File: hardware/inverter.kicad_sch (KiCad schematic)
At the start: 18 parts, among them U2 DRV8262DDWR, U3 TLC555IDR

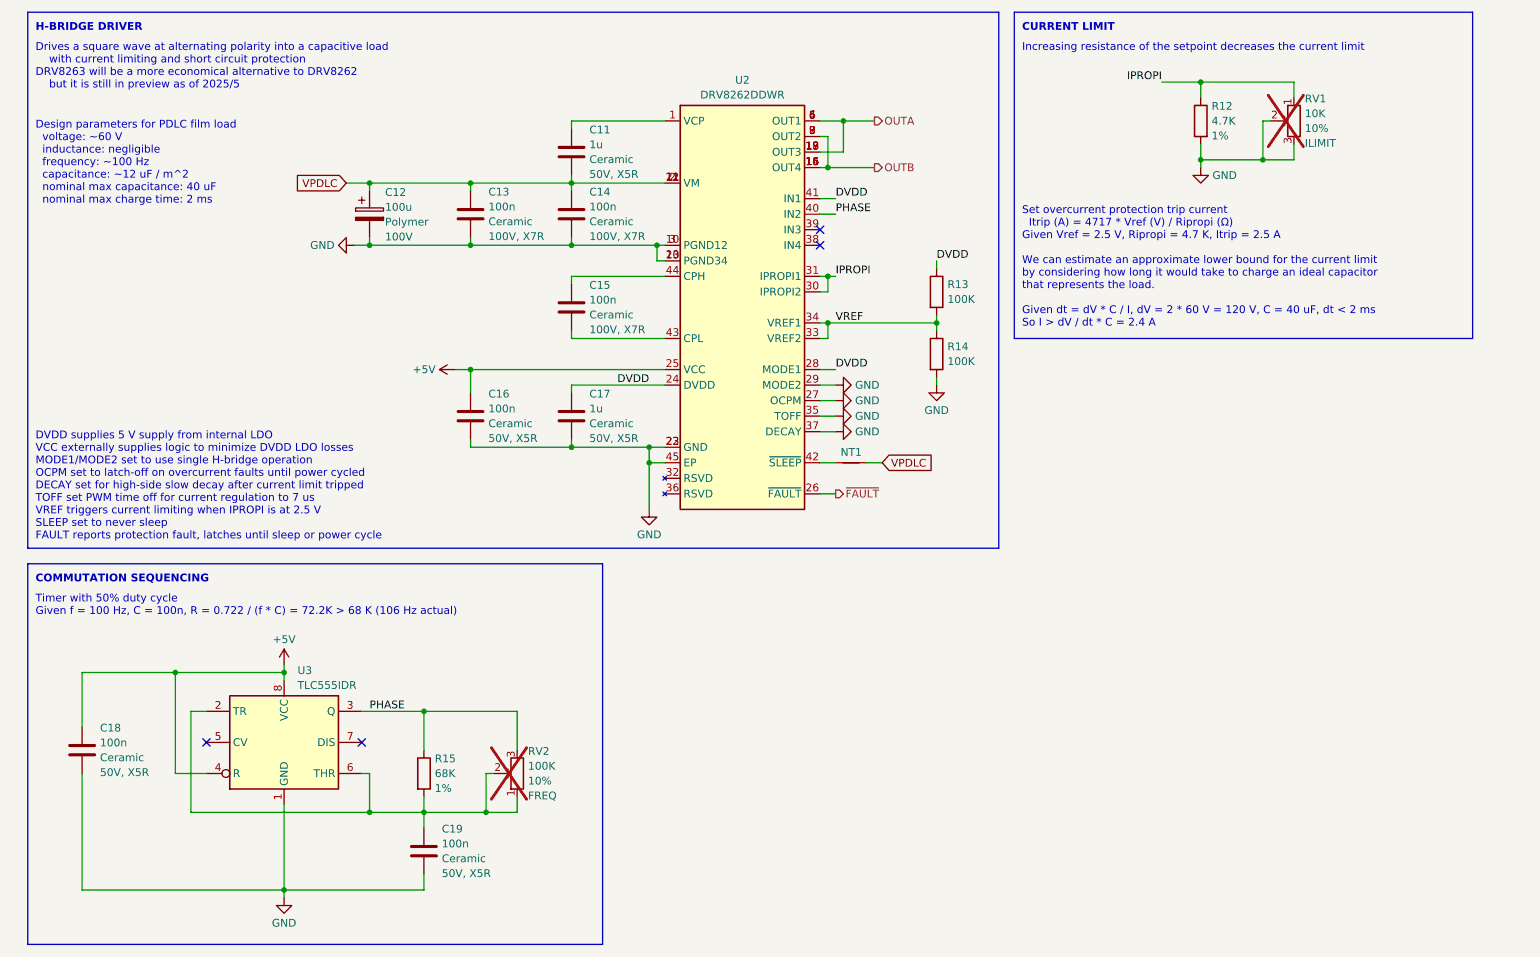
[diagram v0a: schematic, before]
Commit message: Revised layout using LM5108 and discrete FETs
LM5108 is less expensive but it requires more board area.  In lieu of
active current limiting, we rely on the LM5158 hiccup overload
protection.  The FETs are intentionally oversized to handle large
current pulses when switching the polarity of the capacitive load.

This design is complete and ready for manufacture.
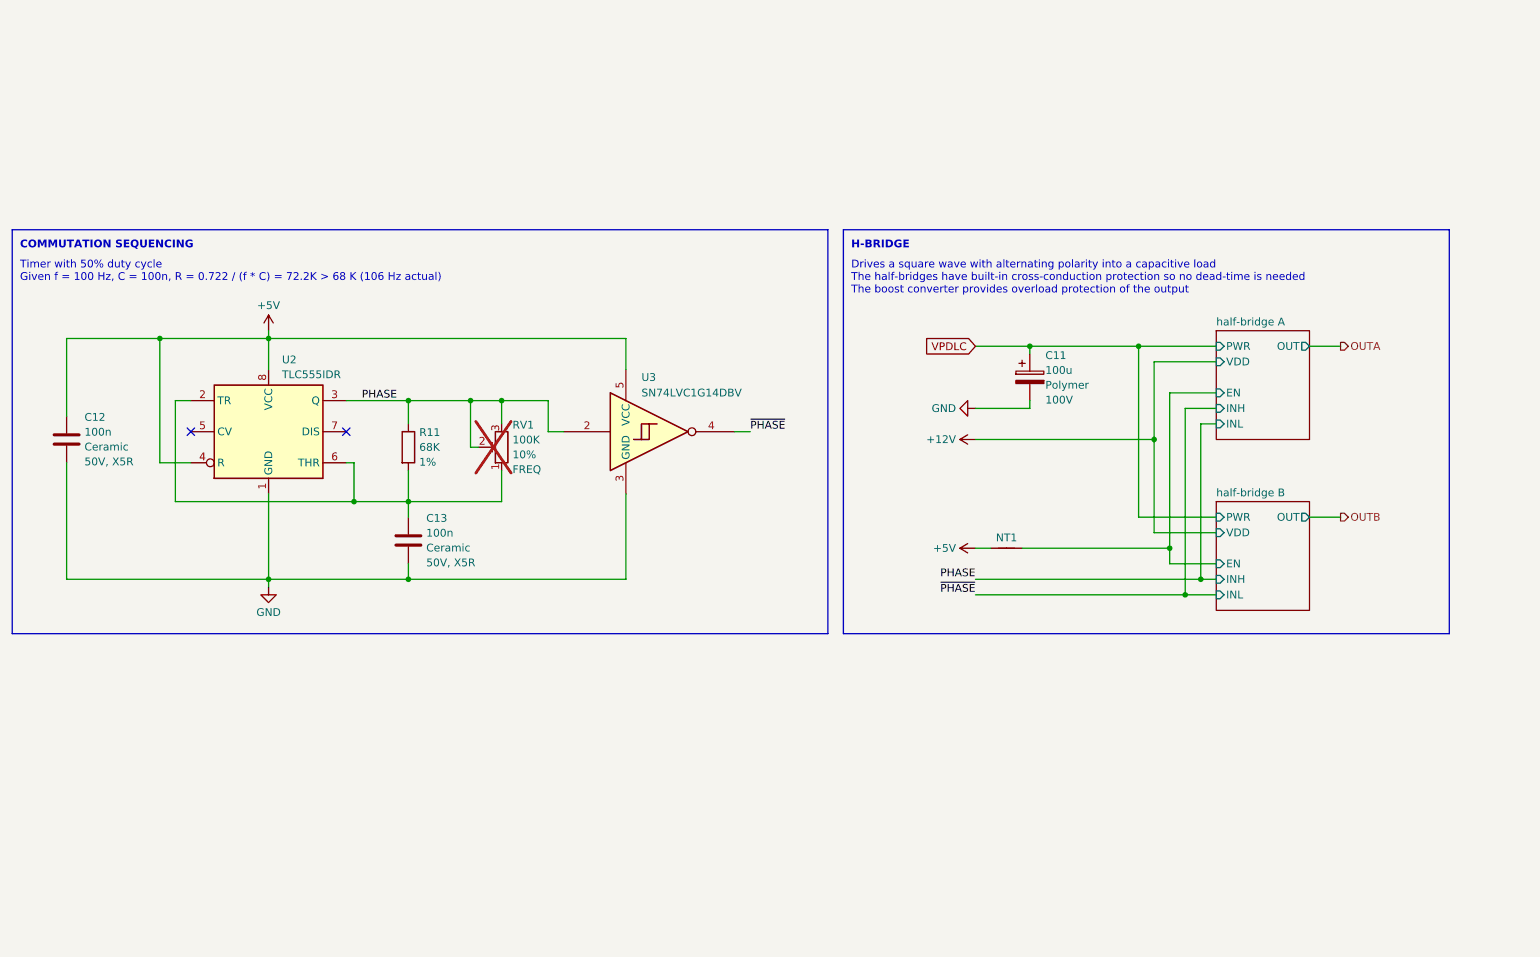
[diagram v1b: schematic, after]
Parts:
- removed C11, C17: 1u, Capacitor_SMD:C_0603_1608Metric, symbol Device:C
- removed C12: 100u, Capacitor_THT:CP_Radial_D10.0mm_P5.00mm, symbol Device:C_Polarized
- removed C13, C14, C15: 100n, Capacitor_SMD:C_0805_2012Metric, symbol Device:C
- removed C16: 100n, Capacitor_SMD:C_0603_1608Metric, symbol Device:C
- removed R12: 4.7K, Resistor_SMD:R_0603_1608Metric, symbol Device:R
- removed R13, R14: 100K, Resistor_SMD:R_0603_1608Metric, symbol Device:R
- removed RV1: 10K, 3362P-1-502LF:TRIM_3362P-1-502LF, symbol Device:R_Potentiometer_Trim
- removed U2: DRV8262DDWR, Package_SO:HTSSOP-44-1EP_6.1x14mm_P0.635mm_EP5.2x14mm_Mask4.31x8.26mm, symbol DRV8262:DRV8262DDWR
- added C11: 100u, Capacitor_THT:CP_Radial_D10.0mm_P5.00mm, symbol Device:C_Polarized
- added U3: SN74LVC1G14DBV, Package_TO_SOT_SMD:SOT-23-5, symbol 74xGxx:SN74LVC1G14DBV
- renumbered C18 to C12, C19 to C13, R15 to R11, RV2 to RV1, U3 to U2
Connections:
- net +5V: now also NT1.1, U3.5 (VCC)
- net GND: now also C11.2, U3.3 (GND)
- net PHASE: now also RV1.2, U3.2
- net VPDLC: now also C11.1; no longer NT1.2
- net at C13.1, R11.2, RV1.1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: no longer RV1.2
- new net half-bridge A/EN: NT1.2
- new net ~{PHASE}: U3.4
- no-connect marks 4 -> 2
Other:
- added sheet half-bridge A (half-bridge.kicad_sch)
- added sheet half-bridge B (half-bridge.kicad_sch)
- note added: "Drives a square wave with alternating polarity into a capacitive load The half-bridges have built-in cross-conduction protection so no dead-time is needed The boost converter provides overload protection of the output"
- note added: "H-BRIDGE"
- note removed: "CURRENT LIMIT"
- note removed: "DVDD supplies 5 V supply from internal LDO VCC externally supplies logic to minimize DVDD LDO losses MODE1/MODE2 set to use single H-bridge operation OCPM set to latch-off on overcurrent faults until power cycled DECAY set for high-side slow decay after current limit tripped TOFF set PWM time off for current regulation to 7 us VREF triggers current limiting when IPROPI is at 2.5 V SLEEP set to ne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"
- note removed: "Design parameters for PDLC film load voltage: ~60 V inductance: negligible frequency: ~100 Hz capacitance: ~12 uF / m^2 nominal max capacitance: 40 uF nominal max charge time: 2 ms"
- note removed: "Drives a square wave at alternating polarity into a capacitive load with current limiting and short circuit protection DRV8263 will be a more economical alternative to DRV8262 but it is still in preview as of 2025/5"
- note removed: "H-BRIDGE DRIVER"
- note removed: "Increasing resistance of the setpoint decreases the current limit"
- note removed: "Set overcurrent protection trip current Itrip (A) = 4717 * Vref (V) / Ripropi (Ω) Given Vref = 2.5 V, Ripropi = 4.7 K, Itrip = 2.5 A We can estimate an approximate lower bound for the current limit by considering how long it would take to charge an ideal capacitor that represents the load. Given dt = dV * C / I, dV = 2 * 60 V = 120 V, C = 40 uF, dt < 2 ms So I > dV / dt * C = 2.4 A"
- moved on the sheet: C12, C13, R11, RV1, U2
